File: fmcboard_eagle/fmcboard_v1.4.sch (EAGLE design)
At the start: 160 parts, among them IC1 OPA699ID, IC10 LTC6229IMS8E#TRPBF, IC11 7805TV, IC12 SN74AUC2G66DCTR, IC13 SN74AUC2G66DCTR, IC14 SN74AUC2G66DCTR, IC15 SN74AUC2G66DCTR, IC16 DAC7578SPWR, IC2 DAC7578SPWR, IC3 LTC6229IMS8E#TRPBF, IC4 LTC6229IMS8E#TRPBF, IC5 LM358, IC6 OPA699ID, IC7 OPA699ID, IC8 LTC6229IMS8E#TRPBF, IC9 LTC6229IMS8E#TRPBF, J1 8pin, J10 8pin, J12 4p-2.54, J2 ASP-134604-01, J3 4p-2.54, J4 4p-2.54, J5 8pin, J6 4p-2.54, J7 4p-2.54, J8 4p-2.54, J9 8pin, U1 TXS0108EPWR, U2 STMICROELECTRONICS_L7905ACVST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

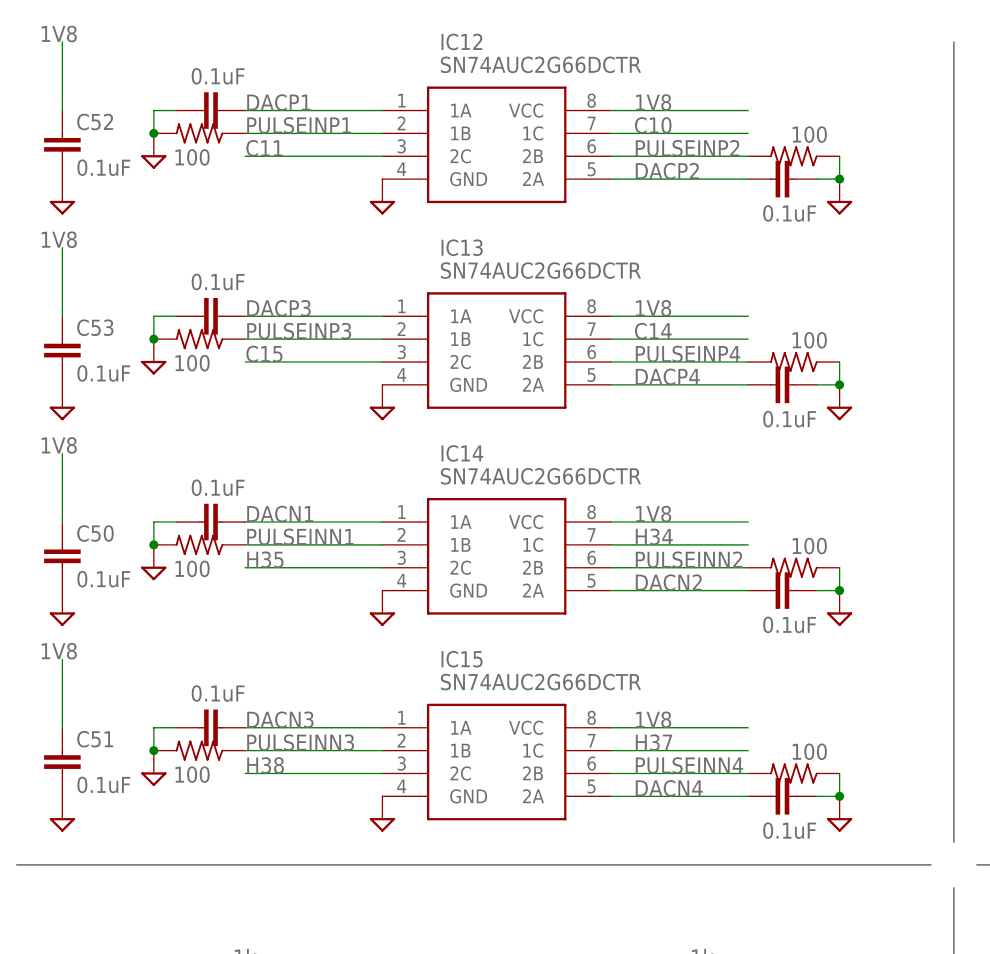
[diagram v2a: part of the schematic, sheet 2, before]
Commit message: v1.43 100 -> 47 Ohm for pulses
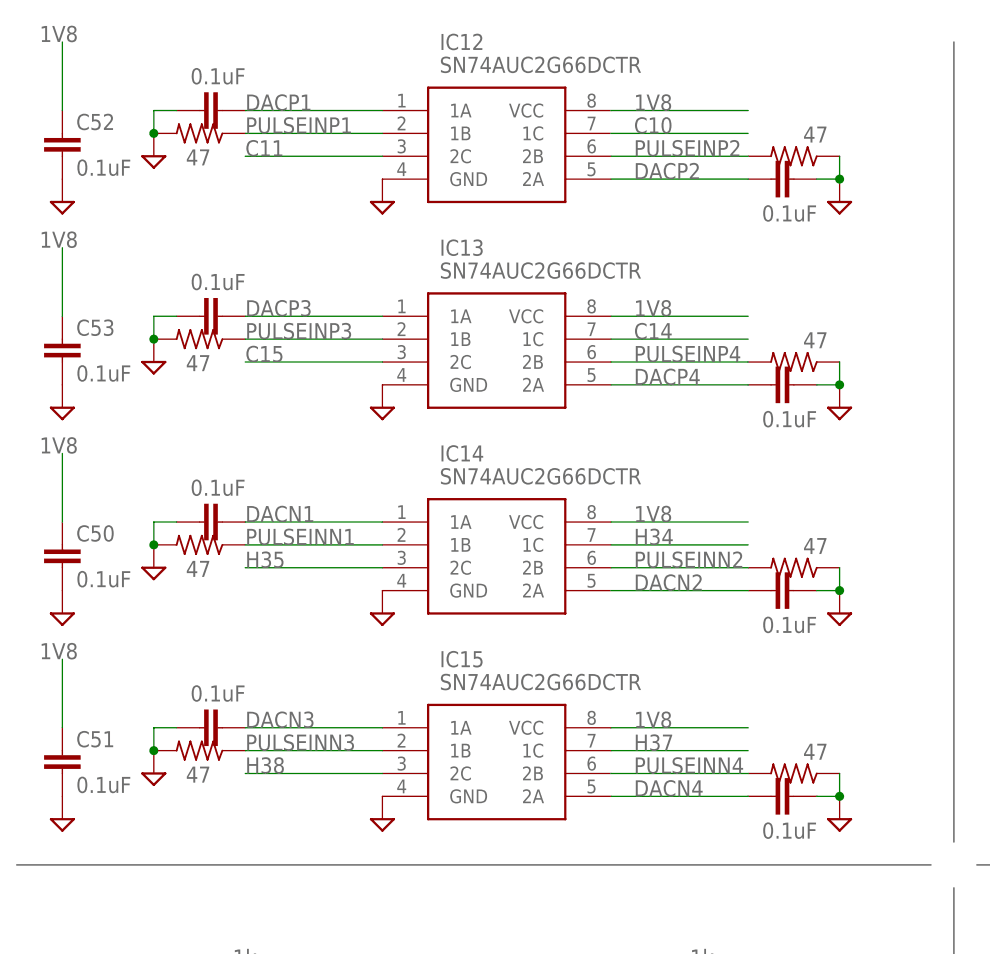
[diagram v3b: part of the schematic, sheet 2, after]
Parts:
- R37, R39, R41, R43, R44, R45, R46, R47: value 100 -> 47
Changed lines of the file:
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@@
 <part name="R35" library="rcl" library_urn="urn:adsk.eagle:library:334" deviceset="R-US_" device="R0805" package3d_urn="urn:adsk.eagle:package:23553/2" value="4k"/>
 <part name="J10" library="SparkFun-Connectors" library_urn="urn:adsk.eagle:library:513" deviceset="CONN_08" device="&quot;" package3d_urn="urn:adsk.eagle:package:38138/1" value="8pin"/>
-<part name="R37" library="rcl" library_urn="urn:adsk.eagle:library:334" deviceset="R-US_" device="R0805" package3d_urn="urn:adsk.eagle:package:23553/2" value="100"/>
-<part name="R39" library="rcl" library_urn="urn:adsk.eagle:library:334" deviceset="R-US_" device="R0805" package3d_urn="urn:adsk.eagle:package:23553/2" value="100"/>
-<part name="R41" library="rcl" library_urn="urn:adsk.eagle:library:334" deviceset="R-US_" device="R0805" package3d_urn="urn:adsk.eagle:package:23553/2" value="100"/>
-<part name="R43" library="rcl" library_urn="urn:adsk.eagle:library:334" deviceset="R-US_" device="R0805" package3d_urn="urn:adsk.eagle:package:23553/2" value="100"/>
-<part name="R44" library="rcl" library_urn="urn:adsk.eagle:library:334" deviceset="R-US_" device="R0805" package3d_urn="urn:adsk.eagle:package:23553/2" value="100"/>
-<part name="R45" library="rcl" library_urn="urn:adsk.eagle:library:334" deviceset="R-US_" device="R0805" package3d_urn="urn:adsk.eagle:package:23553/2" value="100"/>
-<part name="R46" library="rcl" library_urn="urn:adsk.eagle:library:334" deviceset="R-US_" device="R0805" package3d_urn="urn:adsk.eagle:package:23553/2" value="100"/>
-<part name="R47" library="rcl" library_urn="urn:adsk.eagle:library:334" deviceset="R-US_" device="R0805" package3d_urn="urn:adsk.eagle:package:23553/2" value="100"/>
+<part name="R37" library="rcl" library_urn="urn:adsk.eagle:library:334" deviceset="R-US_" device="R0805" package3d_urn="urn:adsk.eagle:package:23553/2" value="47"/>
+<part name="R39" library="rcl" library_urn="urn:adsk.eagle:library:334" deviceset="R-US_" device="R0805" package3d_urn="urn:adsk.eagle:package:23553/2" value="47"/>
+<part name="R41" library="rcl" library_urn="urn:adsk.eagle:library:334" deviceset="R-US_" device="R0805" package3d_urn="urn:adsk.eagle:package:23553/2" value="47"/>
+<part name="R43" library="rcl" library_urn="urn:adsk.eagle:library:334" deviceset="R-US_" device="R0805" package3d_urn="urn:adsk.eagle:package:23553/2" value="47"/>
+<part name="R44" library="rcl" library_urn="urn:adsk.eagle:library:334" deviceset="R-US_" device="R0805" package3d_urn="urn:adsk.eagle:package:23553/2" value="47"/>
+<part name="R45" library="rcl" library_urn="urn:adsk.eagle:library:334" deviceset="R-US_" device="R0805" package3d_urn="urn:adsk.eagle:package:23553/2" value="47"/>
+<part name="R46" library="rcl" library_urn="urn:adsk.eagle:library:334" deviceset="R-US_" device="R0805" package3d_urn="urn:adsk.eagle:package:23553/2" value="47"/>
+<part name="R47" library="rcl" library_urn="urn:adsk.eagle:library:334" deviceset="R-US_" device="R0805" package3d_urn="urn:adsk.eagle:package:23553/2" value="47"/>
 <part name="SUPPLY48" library="supply2" library_urn="urn:adsk.eagle:library:372" deviceset="GND" device=""/>
 <part name="SUPPLY50" library="supply2" library_urn="urn:adsk.eagle:library:372" deviceset="GND" device=""/>

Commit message: v1.43 ordered
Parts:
- R11: value 5k -> 4.7k
- R14, R25, R31: value 4k -> 4.7k
- R2, R34: value 50 -> 47
- R35: value 4k -> 4.7K
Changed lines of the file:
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@@
 <part name="R10" library="rcl" library_urn="urn:adsk.eagle:library:334" deviceset="R-US_" device="R0805" package3d_urn="urn:adsk.eagle:package:23553/2" value="200"/>
 <part name="R13" library="rcl" library_urn="urn:adsk.eagle:library:334" deviceset="R-US_" device="R0805" package3d_urn="urn:adsk.eagle:package:23553/2" value="1k"/>
-<part name="R14" library="rcl" library_urn="urn:adsk.eagle:library:334" deviceset="R-US_" device="R0805" package3d_urn="urn:adsk.eagle:package:23553/2" value="4k"/>
+<part name="R14" library="rcl" library_urn="urn:adsk.eagle:library:334" deviceset="R-US_" device="R0805" package3d_urn="urn:adsk.eagle:package:23553/2" value="4.7k"/>
 <part name="R_O1" library="resistor" library_urn="urn:adsk.eagle:library:348" deviceset="R-TRIMM" device="3296W" package3d_urn="urn:adsk.eagle:package:26033/1" value="20k"/>
 <part name="R3" library="rcl" library_urn="urn:adsk.eagle:library:334" deviceset="R-US_" device="R0805" package3d_urn="urn:adsk.eagle:package:23553/2" value="100k"/>
@@
 <part name="SUPPLY32" library="supply2" library_urn="urn:adsk.eagle:library:372" deviceset="GND" device=""/>
 <part name="SUPPLY21" library="supply2" library_urn="urn:adsk.eagle:library:372" deviceset="GND" device=""/>
-<part name="R11" library="rcl" library_urn="urn:adsk.eagle:library:334" deviceset="R-US_" device="R0805" package3d_urn="urn:adsk.eagle:package:23553/2" value="5k"/>
+<part name="R11" library="rcl" library_urn="urn:adsk.eagle:library:334" deviceset="R-US_" device="R0805" package3d_urn="urn:adsk.eagle:package:23553/2" value="4.7k"/>
 <part name="IC4" library="LTC6229IMS8E#TRPBF" deviceset="LTC6229IMS8E#TRPBF" device=""/>
 <part name="C4" library="SparkFun-Passives" deviceset="CAP" device="0805" value="0.1uF"/>
@@
 <part name="R19" library="rcl" library_urn="urn:adsk.eagle:library:334" deviceset="R-US_" device="R0805" package3d_urn="urn:adsk.eagle:package:23553/2" value="200"/>
 <part name="R20" library="rcl" library_urn="urn:adsk.eagle:library:334" deviceset="R-US_" device="R0805" package3d_urn="urn:adsk.eagle:package:23553/2" value="1k"/>
-<part name="R25" library="rcl" library_urn="urn:adsk.eagle:library:334" deviceset="R-US_" device="R0805" package3d_urn="urn:adsk.eagle:package:23553/2" value="4k"/>
+<part name="R25" library="rcl" library_urn="urn:adsk.eagle:library:334" deviceset="R-US_" device="R0805" package3d_urn="urn:adsk.eagle:package:23553/2" value="4.7k"/>
 <part name="IC7" library="OPA699ID" deviceset="OPA699ID" device=""/>
 <part name="SUPPLY19" library="supply2" library_urn="urn:adsk.eagle:library:372" deviceset="GND" device=""/>
@@
 <part name="R40" library="rcl" library_urn="urn:adsk.eagle:library:334" deviceset="R-US_" device="R0805" package3d_urn="urn:adsk.eagle:package:23553/2" value="1k"/>
 <part name="SUPPLY25" library="supply2" library_urn="urn:adsk.eagle:library:372" deviceset="GND" device=""/>
-<part name="R2" library="rcl" library_urn="urn:adsk.eagle:library:334" deviceset="R-US_" device="R0805" package3d_urn="urn:adsk.eagle:package:23553/2" value="50"/>
+<part name="R2" library="rcl" library_urn="urn:adsk.eagle:library:334" deviceset="R-US_" device="R0805" package3d_urn="urn:adsk.eagle:package:23553/2" value="47"/>
 <part name="C34" library="SparkFun-Passives" deviceset="CAP" device="0805" value="1pF"/>
 <part name="C35" library="SparkFun-Passives" deviceset="CAP" device="0805" value="1pF"/>
@@
 <part name="C32" library="SparkFun-Passives" deviceset="CAP" device="0805" value="1pF"/>
 <part name="C33" library="SparkFun-Passives" deviceset="CAP" device="0805" value="1pF"/>
-<part name="R34" library="rcl" library_urn="urn:adsk.eagle:library:334" deviceset="R-US_" device="R0805" package3d_urn="urn:adsk.eagle:package:23553/2" value="50"/>
+<part name="R34" library="rcl" library_urn="urn:adsk.eagle:library:334" deviceset="R-US_" device="R0805" package3d_urn="urn:adsk.eagle:package:23553/2" value="47"/>
 <part name="R42" library="rcl" library_urn="urn:adsk.eagle:library:334" deviceset="R-US_" device="R0805" package3d_urn="urn:adsk.eagle:package:23553/2" value="50?"/>
 <part name="J8" library="Seeed-Connector" library_urn="urn:adsk.eagle:library:478" deviceset="DIP-BLACK-FEMALE-HEADER-VERT(4P-2.54)" device="" package3d_urn="urn:adsk.eagle:package:33137/1" value="4p-2.54"/>
@@
 <part name="SUPPLY44" library="supply2" library_urn="urn:adsk.eagle:library:372" deviceset="GND" device=""/>
 <part name="SUPPLY46" library="supply2" library_urn="urn:adsk.eagle:library:372" deviceset="GND" device=""/>
-<part name="R31" library="rcl" library_urn="urn:adsk.eagle:library:334" deviceset="R-US_" device="R0805" package3d_urn="urn:adsk.eagle:package:23553/2" value="4k"/>
-<part name="R35" library="rcl" library_urn="urn:adsk.eagle:library:334" deviceset="R-US_" device="R0805" package3d_urn="urn:adsk.eagle:package:23553/2" value="4k"/>
+<part name="R31" library="rcl" library_urn="urn:adsk.eagle:library:334" deviceset="R-US_" device="R0805" package3d_urn="urn:adsk.eagle:package:23553/2" value="4.7k"/>
+<part name="R35" library="rcl" library_urn="urn:adsk.eagle:library:334" deviceset="R-US_" device="R0805" package3d_urn="urn:adsk.eagle:package:23553/2" value="4.7K"/>
 <part name="J10" library="SparkFun-Connectors" library_urn="urn:adsk.eagle:library:513" deviceset="CONN_08" device="&quot;" package3d_urn="urn:adsk.eagle:package:38138/1" value="8pin"/>
 <part name="R37" library="rcl" library_urn="urn:adsk.eagle:library:334" deviceset="R-US_" device="R0805" package3d_urn="urn:adsk.eagle:package:23553/2" value="47"/>
